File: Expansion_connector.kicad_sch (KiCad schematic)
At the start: 0 parts

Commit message: [#82057] Add FMC connector, add grounds for the connector, mark part of the connector overlapping with AGX, add PCIe
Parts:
- added J10: ASP-218650-01_mounting_holes, antmicro-footprints:ASP-218650-01_mounting_holes, symbol antmicroB2BConnectors:ASP-218650-01_mounting_holes
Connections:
- new net GND: J10.A01, J10.A04, J10.A05, J10.A08, J10.A09, J10.A12, J10.A13, J10.A16, J10.A17, J10.A20, J10.A21, J10.A24, J10.A25, J10.A28, J10.A29, J10.A32, J10.A33, J10.A36, J10.A37, J10.A40, J10.B02, J10.B03, J10.B06, J10.B07, J10.B10, J10.B11, J10.B14, J10.B15, J10.B18, J10.B19, J10.B22, J10.B23, J10.B26, J10.B27, J10.B30, J10.B31, J10.B34, J10.B35, J10.B38, J10.B39, J10.C01, J10.C04, J10.C05, J10.C08, J10.C09, J10.C12, J10.C13, J10.C16, J10.C17, J10.C20, J10.C21, J10.C24, J10.C25, J10.C28, J10.C29, J10.C32, J10.C33, J10.C36, J10.C37, J10.C40, J10.D02, J10.D03, J10.D06, J10.D07, J10.D10, J10.D11, J10.D14, J10.D15, J10.D18, J10.D19, J10.D22, J10.D23, J10.D26, J10.D27, J10.D30, J10.D31, J10.D34, J10.D35, J10.D38, J10.D39, J10.E01, J10.E04, J10.E05, J10.E08, J10.E09, J10.E12, J10.E13, J10.E16, J10.E17, J10.E20, J10.E21, J10.E24, J10.E25, J10.E28, J10.E29, J10.E32, J10.E33, J10.E36, J10.E37, J10.E40, J10.F02, J10.F03, J10.F06, J10.F07, J10.F10, J10.F11, J10.F14, J10.F15, J10.F18, J10.F19, J10.F22, J10.F23, J10.F26, J10.F27, J10.F30, J10.F31, J10.F34, J10.F35, J10.F38, J10.F39, J10.G01, J10.G04, J10.G05, J10.G08, J10.G09, J10.G12, J10.G13, J10.G16, J10.G17, J10.G20, J10.G21, J10.G24, J10.G25, J10.G28, J10.G29, J10.G32, J10.G33, J10.G36, J10.G37, J10.G40, J10.H02, J10.H03, J10.H06, J10.H07, J10.H10, J10.H11, J10.H14, J10.H15, J10.H18, J10.H19, J10.H22, J10.H23, J10.H26, J10.H27, J10.H30, J10.H31, J10.H34, J10.H35, J10.H38, J10.H39, J10.J01, J10.J04, J10.J05, J10.J08, J10.J09, J10.J12, J10.J13, J10.J16, J10.J17, J10.J20, J10.J21, J10.J24, J10.J25, J10.J28, J10.J29, J10.J32, J10.J33, J10.J36, J10.J37, J10.J40, J10.K02, J10.K03, J10.K06, J10.K07, J10.K10, J10.K11, J10.K14, J10.K15, J10.K18, J10.K19, J10.K22, J10.K23, J10.K26, J10.K27, J10.K30, J10.K31, J10.K34, J10.K35, J10.K38, J10.K39, J10.M05, J10.M06, J10.M07, J10.M08, J10.M09, J10.M10, J10.M11, J10.M12, J10.M13, J10.M14, J10.M15, J10.M16, J10.M17, J10.M18, J10.M19, J10.M20, J10.M21, J10.M22, J10.M23, J10.M24, J10.M25, J10.M26, J10.M27, J10.M28, J10.M29, J10.M30, J10.M31, J10.M32, J10.M33, J10.M34, J10.M35, J10.M36, J10.M37, J10.M38, J10.M39, J10.M40, J10.Y01, J10.Y04, J10.Y05, J10.Y08, J10.Y09, J10.Y12, J10.Y13, J10.Y16, J10.Y17, J10.Y20, J10.Y21, J10.Y24, J10.Y25, J10.Y28, J10.Y29, J10.Y32, J10.Y33, J10.Y36, J10.Y37, J10.Y40, J10.Z02, J10.Z03, J10.Z06, J10.Z07, J10.Z10, J10.Z11, J10.Z14, J10.Z15, J10.Z18, J10.Z19, J10.Z22, J10.Z23, J10.Z26, J10.Z27, J10.Z30, J10.Z31, J10.Z34, J10.Z35, J10.Z38, J10.Z39
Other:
- note added: "----CSI----"
- note added: "----PCIE----"
- note added: "----RGMII----"
- note added: "65 L K ... B A 64 . : 2 1"
- note added: "AGX"
- note added: "Currnet rating 2.7A 339VDC"
- note added: "FMC"
- note added: "M 40 39 38 ... 4 3 2 1 L K . : B A Z Y"
- note added: "Perypherials"
- note added: "Swap according to AGX pin order"
- note added: "We can change FMC pinout according to how hard it woud be to route it"
- note added: "Will be under AGX"
- note added: "Z1 Y6 ... Y1"

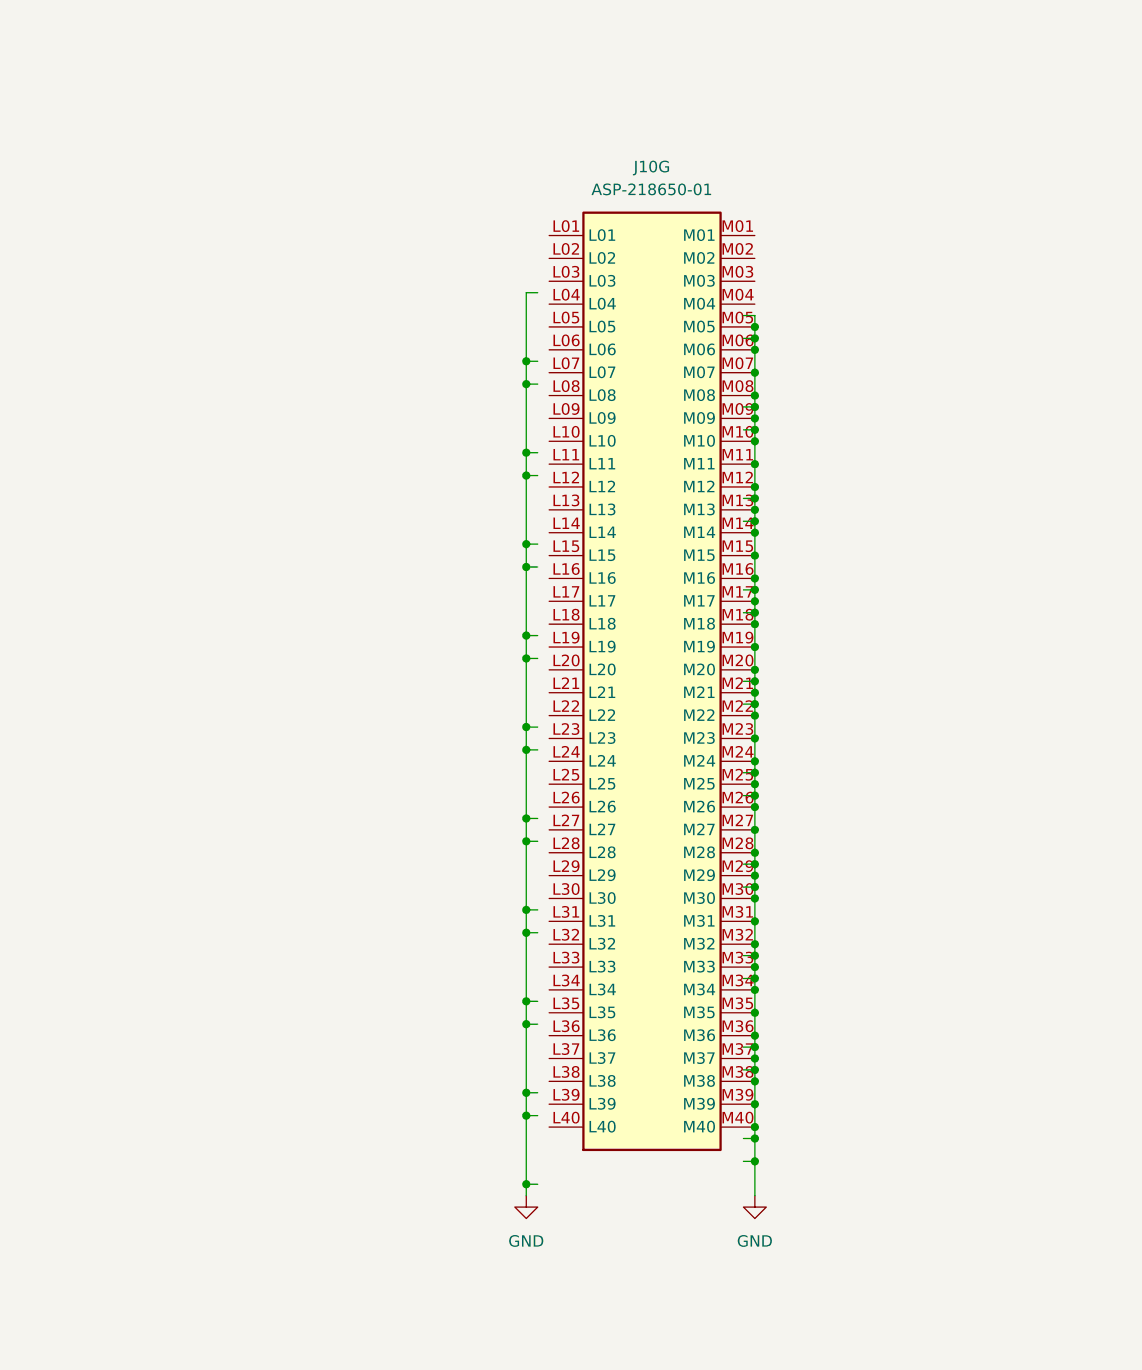
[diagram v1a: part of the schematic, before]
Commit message: [#82057] Route SDIO
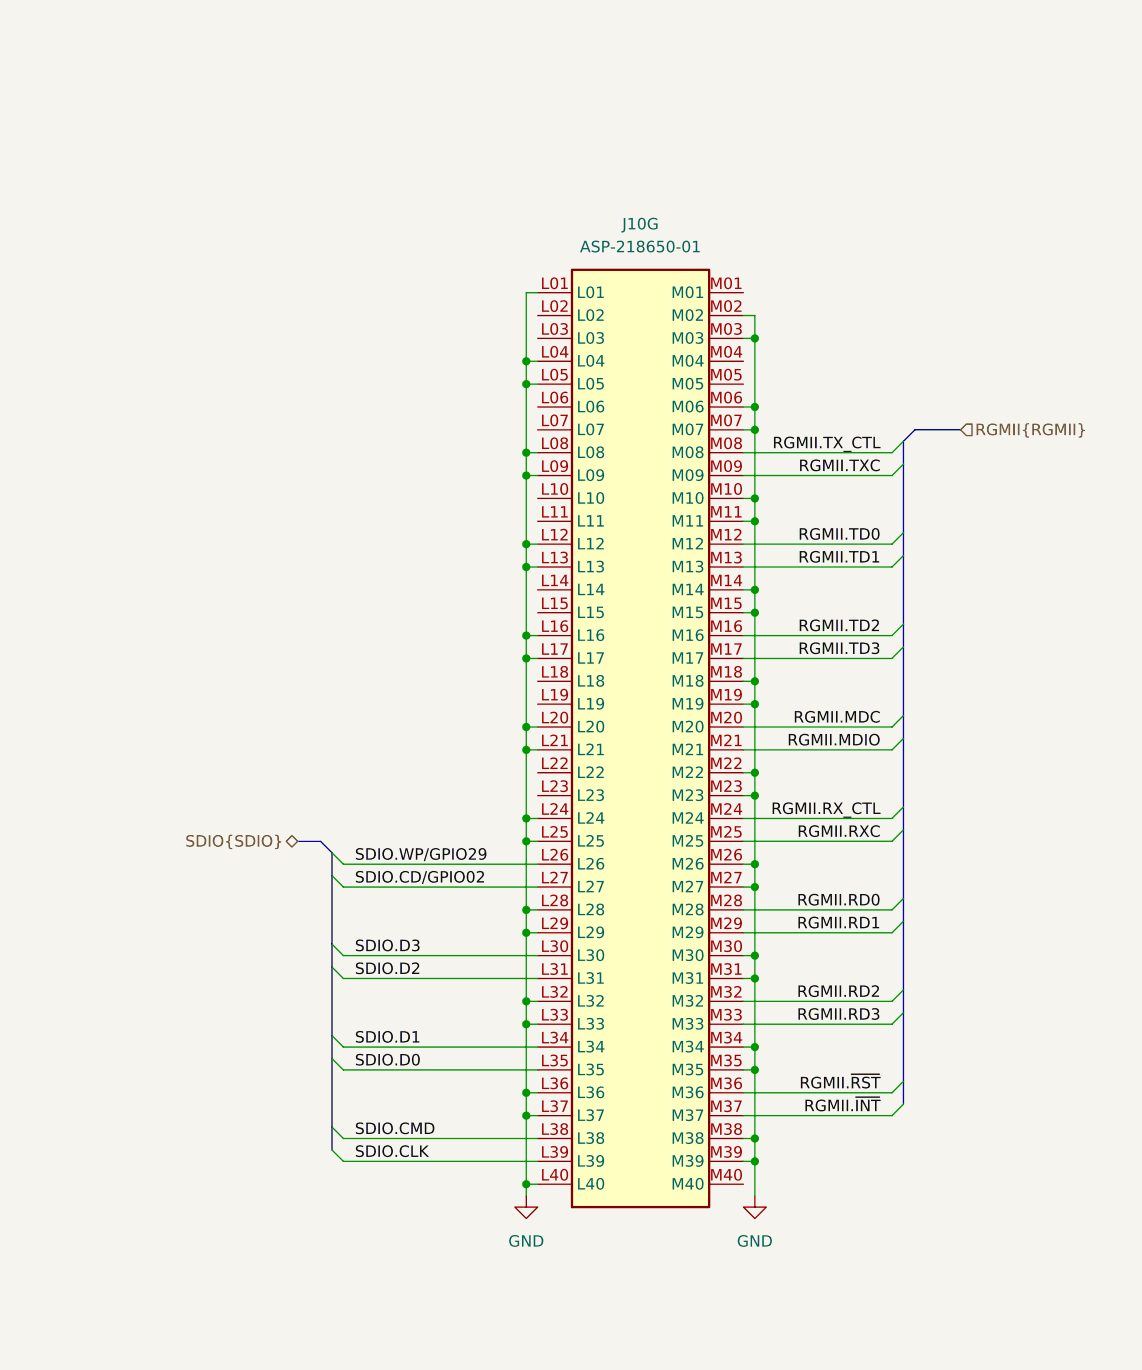
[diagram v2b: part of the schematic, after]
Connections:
- net GND: now also J10.L01, J10.L04, J10.L05, J10.L08, J10.L09, J10.L12, J10.L13, J10.L16, J10.L17, J10.L20, J10.L21, J10.L24, J10.L25, J10.L28, J10.L29, J10.L32, J10.L33, J10.L36, J10.L37, J10.L40, J10.M02, J10.M03; no longer J10.M05, J10.M08, J10.M09, J10.M12, J10.M13, J10.M16, J10.M17, J10.M20, J10.M21, J10.M24, J10.M25, J10.M28, J10.M29, J10.M32, J10.M33, J10.M36, J10.M37, J10.M40
- net SDIO.WP/GPIO29: now reaches J10.L26
- net SDIO.CD/GPIO02: now reaches J10.L27
- net SDIO.D3: now reaches J10.L30
- net SDIO.D2: now reaches J10.L31
- net SDIO.D1: now reaches J10.L34
- net SDIO.D0: now reaches J10.L35
- net SDIO.CMD: now reaches J10.L38
- net SDIO.CLK: now reaches J10.L39
- new net RGMII.MDC: J10.M20
- new net RGMII.MDIO: J10.M21
- new net RGMII.RD0: J10.M28
- new net RGMII.RD1: J10.M29
- new net RGMII.RD2: J10.M32
- new net RGMII.RD3: J10.M33
- new net RGMII.RXC: J10.M25
- new net RGMII.RX_CTL: J10.M24
- new net RGMII.TD0: J10.M12
- new net RGMII.TD1: J10.M13
- new net RGMII.TD2: J10.M16
- new net RGMII.TD3: J10.M17
- new net RGMII.TXC: J10.M09
- new net RGMII.TX_CTL: J10.M08
- new net RGMII.~{INT}: J10.M37
- new net RGMII.~{RST}: J10.M36
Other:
- moved on the sheet: J10G

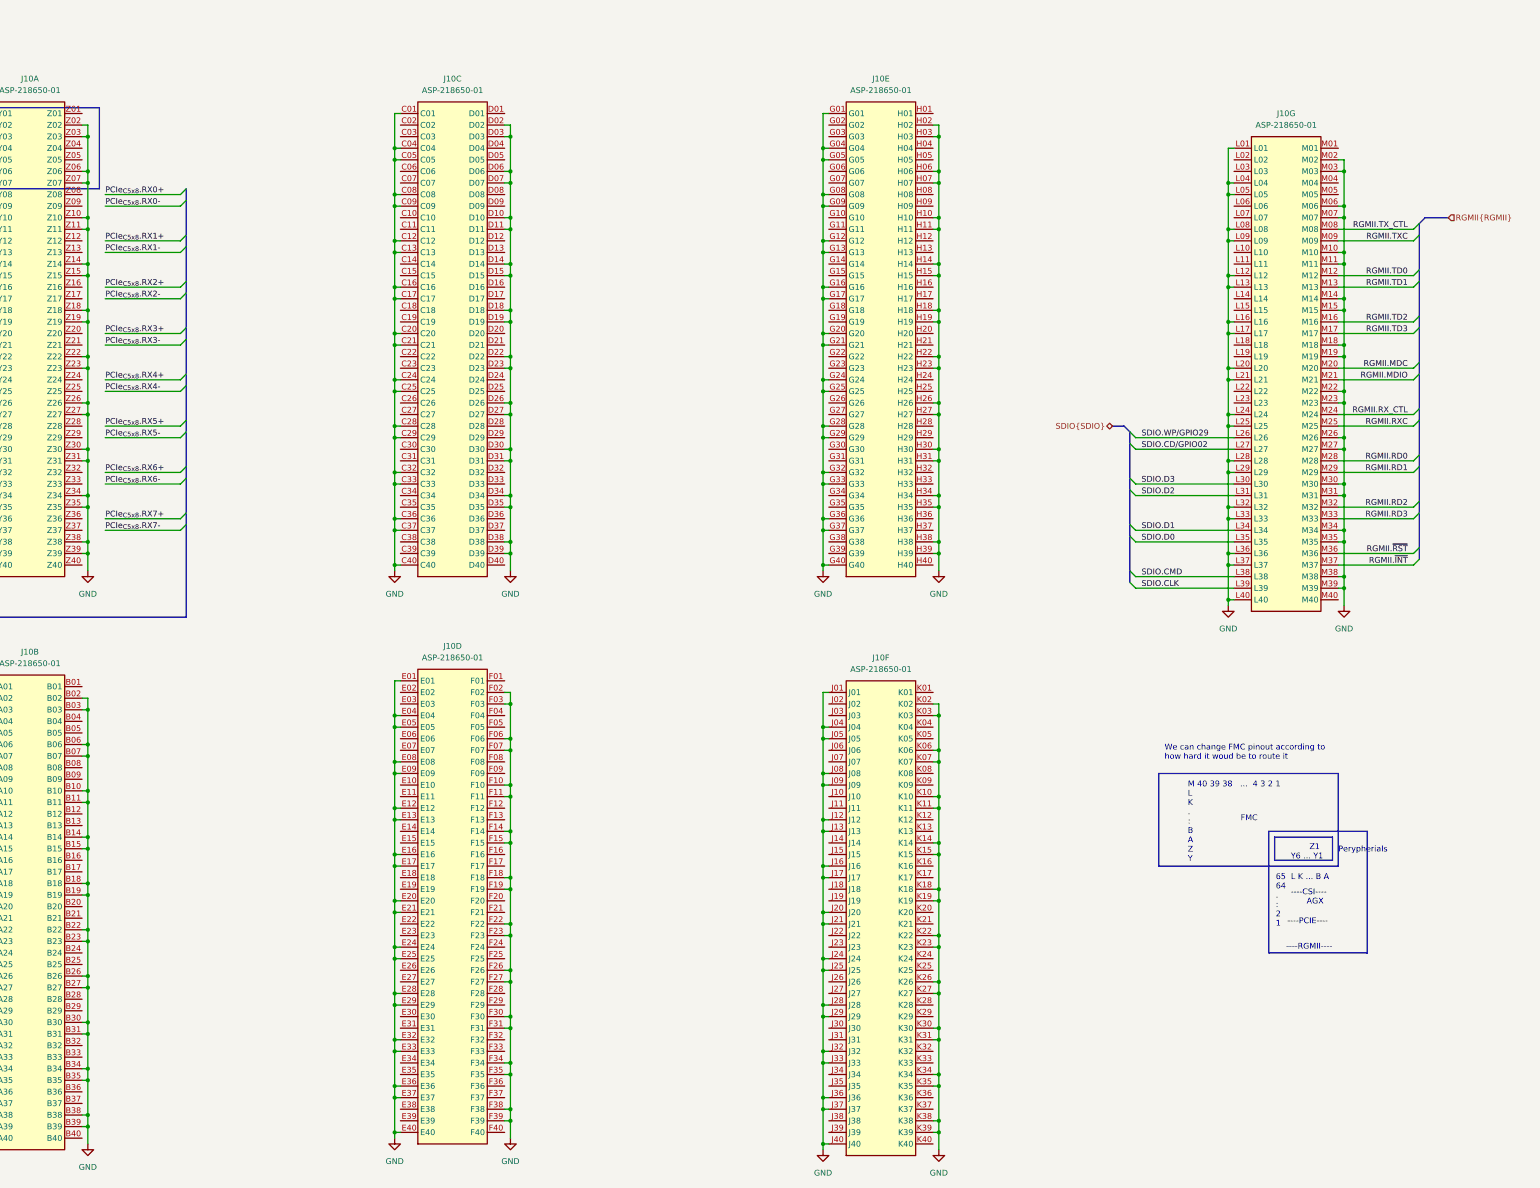
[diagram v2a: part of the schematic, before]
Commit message: [#82057] Route UART, SPI, I2S and unused GPIO on SoM and Expansion connector schematics
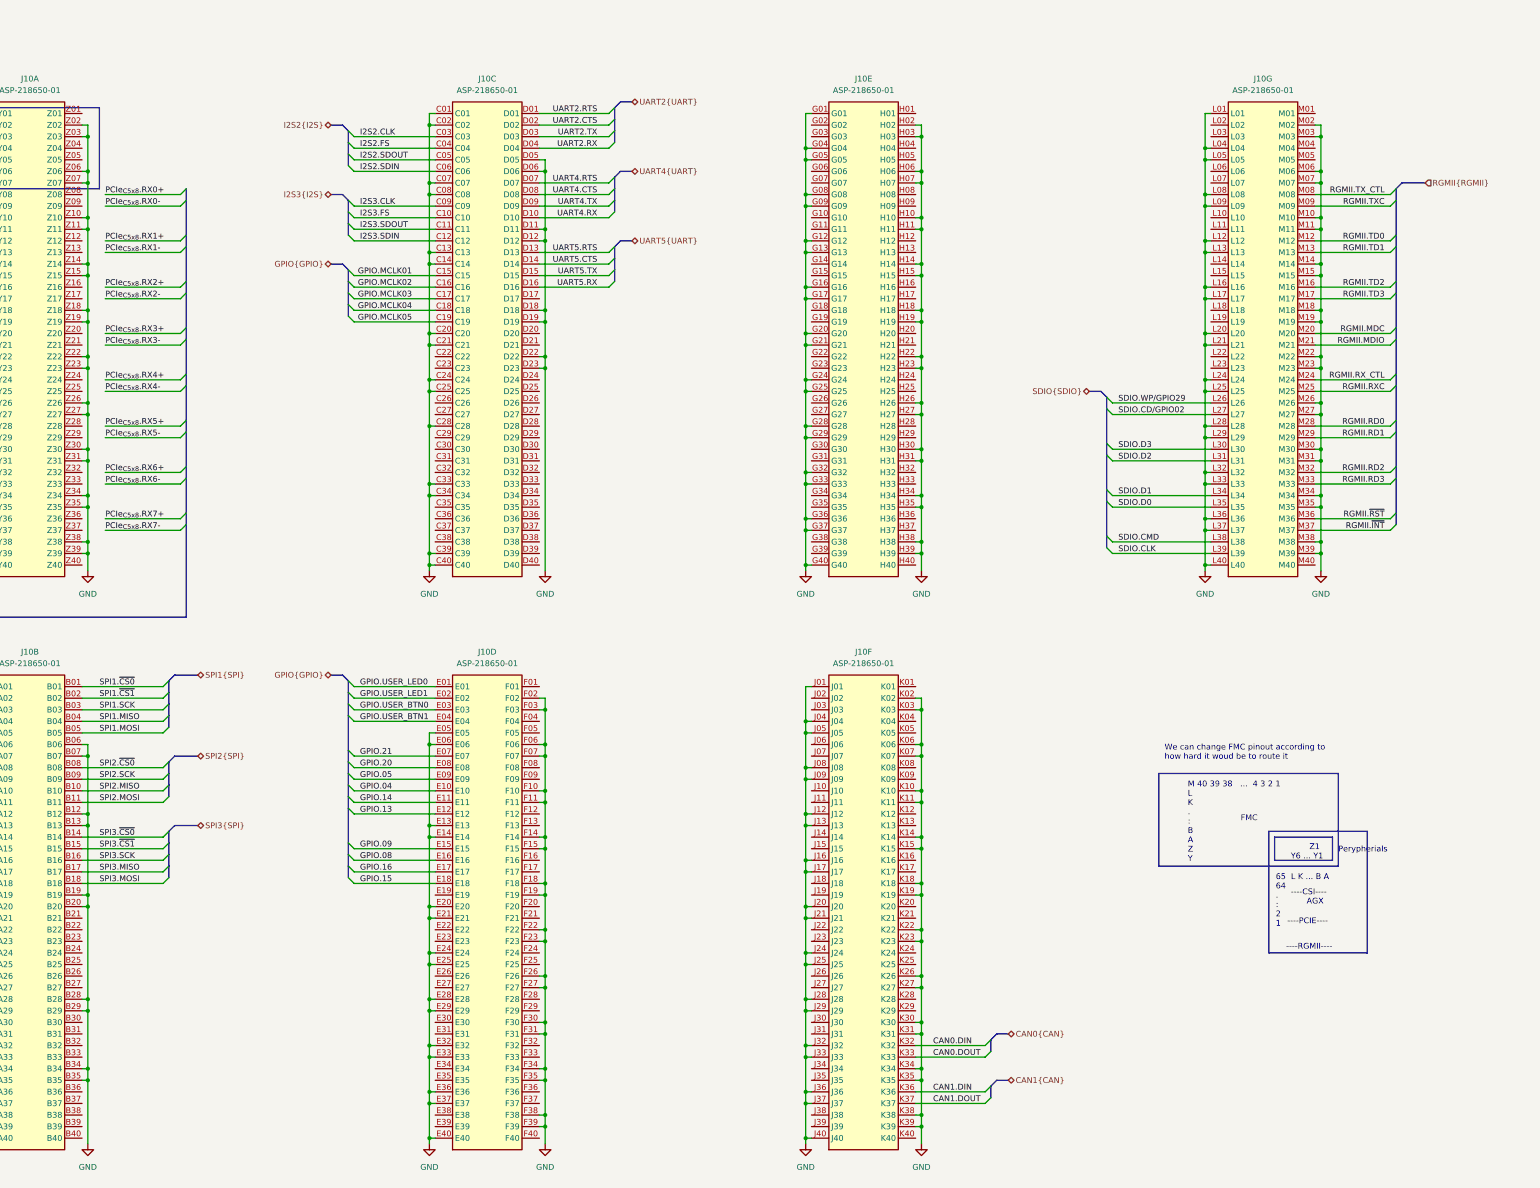
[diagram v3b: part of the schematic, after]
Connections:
- net GND: now also J10.B12, J10.B13, J10.B20, J10.B28, J10.B29, J10.C02, J10.C07, J10.C14, J10.C34, J10.C39, J10.D05, J10.D12, J10.E06, J10.E14; no longer J10.B02, J10.B03, J10.B10, J10.B11, J10.B14, J10.B15, J10.B18, J10.B22, J10.B23, J10.B26, J10.B27, J10.B30, J10.B31, J10.B38, J10.B39, J10.C04, J10.C05, J10.C09, J10.C12, J10.C16, J10.C17, J10.C29, J10.C32, J10.C36, J10.C37, J10.D02, J10.D03, J10.D07, J10.D10, J10.D14, J10.D15, J10.D26, J10.D27, J10.D30, J10.D31, J10.D34, J10.D35, J10.D38, J10.D39, J10.E01, J10.E04, J10.E08, J10.E09, J10.E12, J10.E16, J10.E17
- net GPIO.USER_LED1: now reaches J10.E02
- net GPIO.USER_BTN0: now reaches J10.E03
- net GPIO.21: now reaches J10.E07
- net GPIO.04: now reaches J10.E10
- net GPIO.14: now reaches J10.E11
- net GPIO.09: now reaches J10.E15
- net GPIO.15: now reaches J10.E18
- net CAN0.DIN: now reaches J10.K32
- net CAN0.DOUT: now reaches J10.K33
- net CAN1.DIN: now reaches J10.K36
- net CAN1.DOUT: now reaches J10.K37
- net SPI1.~{CS0}: now reaches J10.B01
- net SPI1.MISO: now reaches J10.B04
- net SPI1.MOSI: now reaches J10.B05
- net SPI2.~{CS0}: now reaches J10.B08
- net SPI2.SCK: now reaches J10.B09
- net SPI3.SCK: now reaches J10.B16
- net SPI3.MISO: now reaches J10.B17
- net I2S2.CLK: now reaches J10.C03
- net I2S2.SDIN: now reaches J10.C06
- net I2S3.FS: now reaches J10.C10
- net I2S3.SDOUT: now reaches J10.C11
- net GPIO.MCLK01: now reaches J10.C15
- net GPIO.MCLK04: now reaches J10.C18
- net GPIO.MCLK05: now reaches J10.C19
- net UART2.RTS: now reaches J10.D01
- net UART2.RX: now reaches J10.D04
- net UART4.CTS: now reaches J10.D08
- net UART4.TX: now reaches J10.D09
- net UART5.RTS: now reaches J10.D13
- net UART5.RX: now reaches J10.D16
- new net GPIO.05: J10.E09
- new net GPIO.08: J10.E16
- new net GPIO.13: J10.E12
- new net GPIO.16: J10.E17
- new net GPIO.20: J10.E08
- new net GPIO.MCLK02: J10.C16
- new net GPIO.MCLK03: J10.C17
- new net GPIO.USER_BTN1: J10.E04
- new net GPIO.USER_LED0: J10.E01
- new net I2S2.FS: J10.C04
- new net I2S2.SDOUT: J10.C05
- new net I2S3.CLK: J10.C09
- new net I2S3.SDIN: J10.C12
- new net SPI1.SCK: J10.B03
- new net SPI1.~{CS1}: J10.B02
- new net SPI2.MISO: J10.B10
- new net SPI2.MOSI: J10.B11
- new net SPI3.MOSI: J10.B18
- new net SPI3.~{CS0}: J10.B14
- new net SPI3.~{CS1}: J10.B15
- new net UART2.CTS: J10.D02
- new net UART2.TX: J10.D03
- new net UART4.RTS: J10.D07
- new net UART4.RX: J10.D10
- new net UART5.CTS: J10.D14
- new net UART5.TX: J10.D15
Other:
- moved on the sheet: J10C, J10D, J10E, J10F, J10G
